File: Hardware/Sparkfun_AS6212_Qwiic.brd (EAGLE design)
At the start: 25.4 x 25.4 mm, 57 parts, among them J1 PTH, J2 QWIIC_RA, J3 QWIIC_RA, U2 AS6212

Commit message: Layout ready for review
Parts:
- removed JP6: JUMPER-SMT_3_1-NC_TRACE_NO-SILK, SparkFun-Jumpers:SMT-JUMPER_3_1-NC_TRACE_NO-SILK
- removed JP7: JUMPER-SMT_3_NO_NO_SILK, SparkFun-Jumpers:SMT-JUMPER_3_0-NO_TRACE_NO-SILK
- removed U$20: (no value), Labels:PWR-()-04
- removed U$21: (no value), Labels:I_SUPER2_C-()-04
- removed U$32, U$37: (no value), output:#ALRT#0
- removed U$42: (no value), buzzard_labels (26):0X480
- added JP10: JUMPER-SMT_3_1-NC_TRACE_NO-SILK, SparkFun-Jumpers:SMT-JUMPER_3_1-NC_TRACE_NO-SILK
- added JP11: JUMPER-SMT_3_NO_NO_SILK, SparkFun-Jumpers:SMT-JUMPER_3_0-NO_TRACE_NO-SILK
- added U$10: (no value), output:SDA6
- added U$11, U$12: (no value), output:#ALRT#AD1#12
- added U$13: (no value), output:VCC4
- added U$14, U$9: (no value), output:GND5
- added U$19: (no value), output:PWR12
- added U$4: (no value), output:#AD0#1
- added U$5: (no value), output:#AD1#1
- added U$6: (no value), output:SCL3
- U$1: device output:TEMPERATURE_SENSOR7 -> output:#LED#10
- U$16: device buzzard_labels (25):0X4A2 -> output:SENSOR8
- U$17: device buzzard_labels (25):0X4B3 -> output:TEMP9
- U$18: device buzzard_labels (1):ADDR0 -> output:0X4812
- U$2: device buzzard_labels (25):0X491 -> output:#I2C#11
- U$7: device Labels:INT-()-04 -> output:VCC4
- U$8: device buzzard_labels (5):LED0 -> output:DEFAULT#11
- moved R6 64.5 mm to (22.9, 19.6), turned to 180 degrees
- moved U$1 53.1 mm to (2.77, 7.44)
- moved U$3 50.1 mm to (4.65, 12.5)
- moved U$18 20.2 mm to (4.70, 9.60), turned to 0 degrees
- moved U$15 19.0 mm to (3.17, 17.3)
- moved U$17 18.9 mm to (4.62, 15.6), turned to 0 degrees
- moved R2 16.6 mm to (23.0, 17.8), turned to 180 degrees
- moved U$16 16.3 mm to (4.55, 14.2), turned to 0 degrees
- moved U$2 10.0 mm to (22.9, 7.57), turned to 0 degrees
- moved U$7 9.93 mm to (21.2, 20.3)
- moved LOGO1 8.20 mm to (10.6, 20.6)
- moved JP1 5.98 mm to (2.77, 5.71), turned to 180 degrees
- moved LOGO2 5.22 mm to (8.48, 18.1)
- moved JP4 3.55 mm to (17.4, 14.5), turned to 270 degrees
- moved U$8 2.82 mm to (4.57, 11.0)
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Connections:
- net ALERT/ADD1: now also JP10.2, JP11.2; no longer JP6.2, JP7.2
- net GND: now also JP11.3; no longer JP6.3
- net N$5: now also JP10.3; no longer JP7.1
- net SCL: now also JP10.1; no longer JP7.3
- net SDA: now also JP11.1; no longer JP6.1
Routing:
- net SCL: track 0.00 -> 63.3 mm, vias 0 -> 4
- net 3.3V: track 0.00 -> 61.5 mm, vias 0 -> 2
- net ALERT/ADD1: track 0.00 -> 60.3 mm, vias 0 -> 2
- net SDA: track 0.00 -> 48.9 mm, vias 0 -> 4
- net ADD0: track 0.00 -> 27.7 mm, vias 0 -> 1
- net N$7: track 0.00 -> 5.97 mm, vias 0 -> 1
- net N$3: track 0.00 -> 5.67 mm, vias 0 -> 1
- net N$5: track 0.00 -> 4.73 mm, vias 0 -> 1
- net N$2: track 0.00 -> 3.52 mm, vias 0 -> 1
- net N$8: track 0.00 -> 2.49 mm, vias 0 -> 1
- net N$1: track 0.00 -> 1.50 mm
- net GND: track 0.00 -> 1.14 mm, vias 0 -> 9
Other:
- outline, holes or cut-outs redrawn

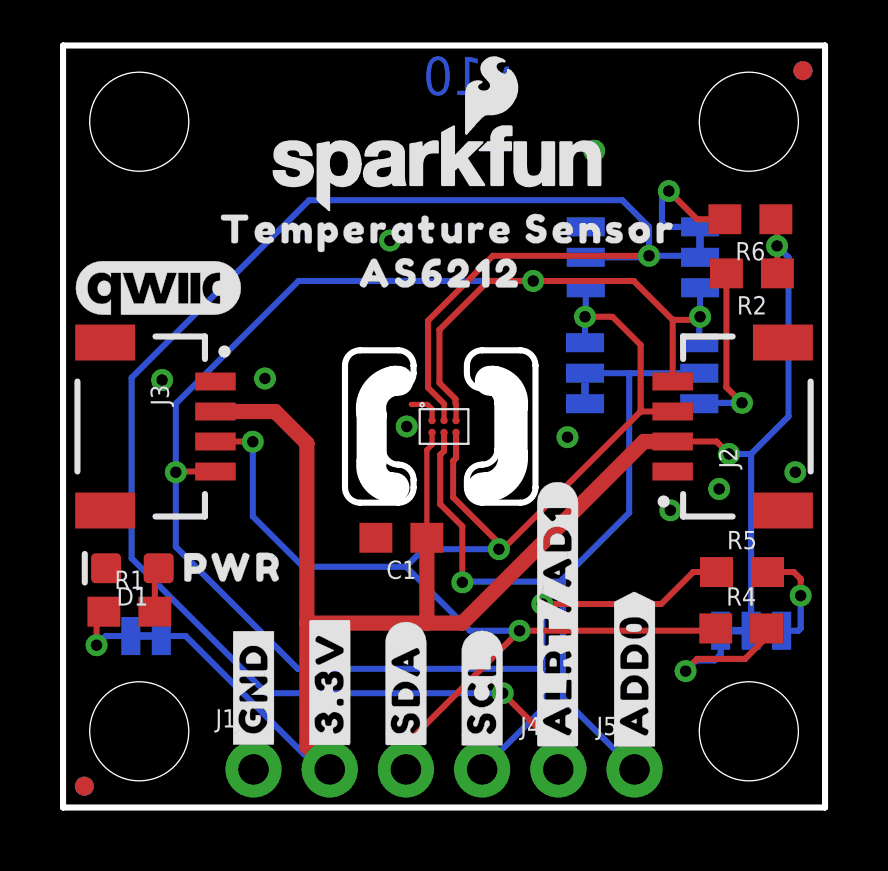
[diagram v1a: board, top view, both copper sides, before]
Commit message: my run of checklist catches
-silk outline of IC package increased to 8 mil
-approved DRC errors
-re-routed off IS to allow GND flow
-more GND stiching vias
-nudged some resistors away from standoff screw head
-updated 3-pad jumpers to latest in library to avoid access DRC errors
-added measures
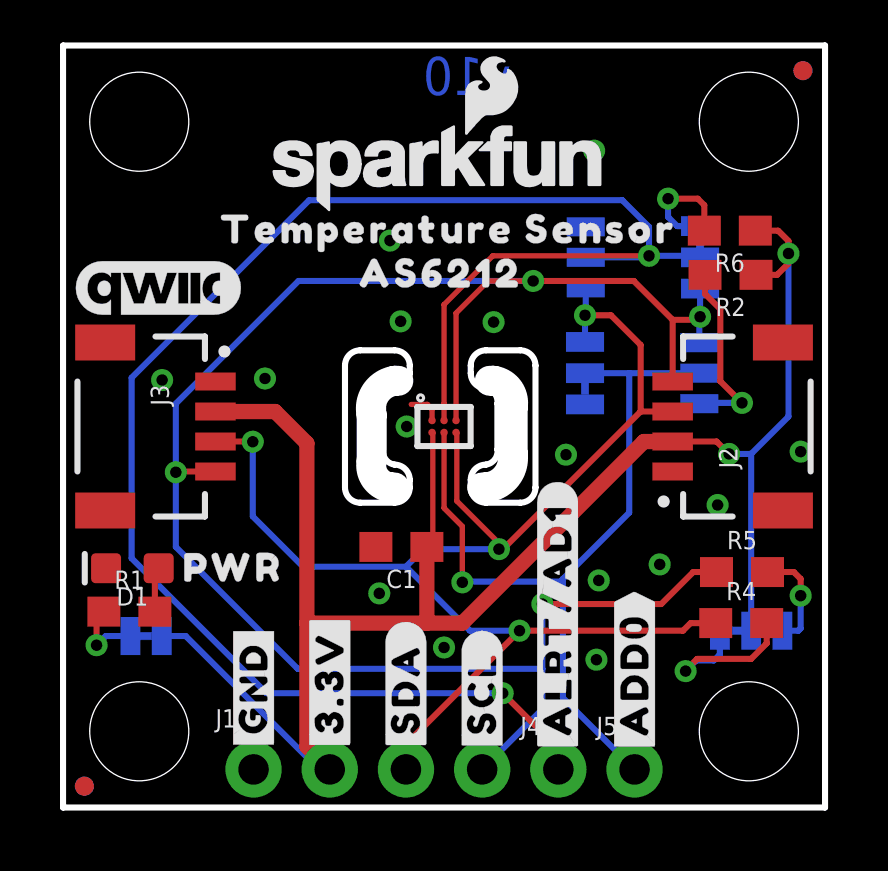
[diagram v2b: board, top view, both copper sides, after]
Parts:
- moved U$8 16.6 mm to (21.2, 10.9)
- moved U$18 16.5 mm to (21.2, 9.32)
- moved FRAME1 10.2 mm to (-7.62, -19.1)
- moved R6 0.78 mm to (22.2, 19.2)
- moved R2 0.71 mm to (22.3, 17.8)
- moved C1 0.30 mm to (11.3, 8.69)
- moved R4 0.18 mm to (22.6, 6.15)
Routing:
- net 3.3V: track 61.5 -> 62.4 mm
- net N$5: track 4.73 -> 3.95 mm
- net GND: vias 9 -> 15
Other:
- outline, holes or cut-outs redrawn
- board text added: "Measurement Units: INCHES"

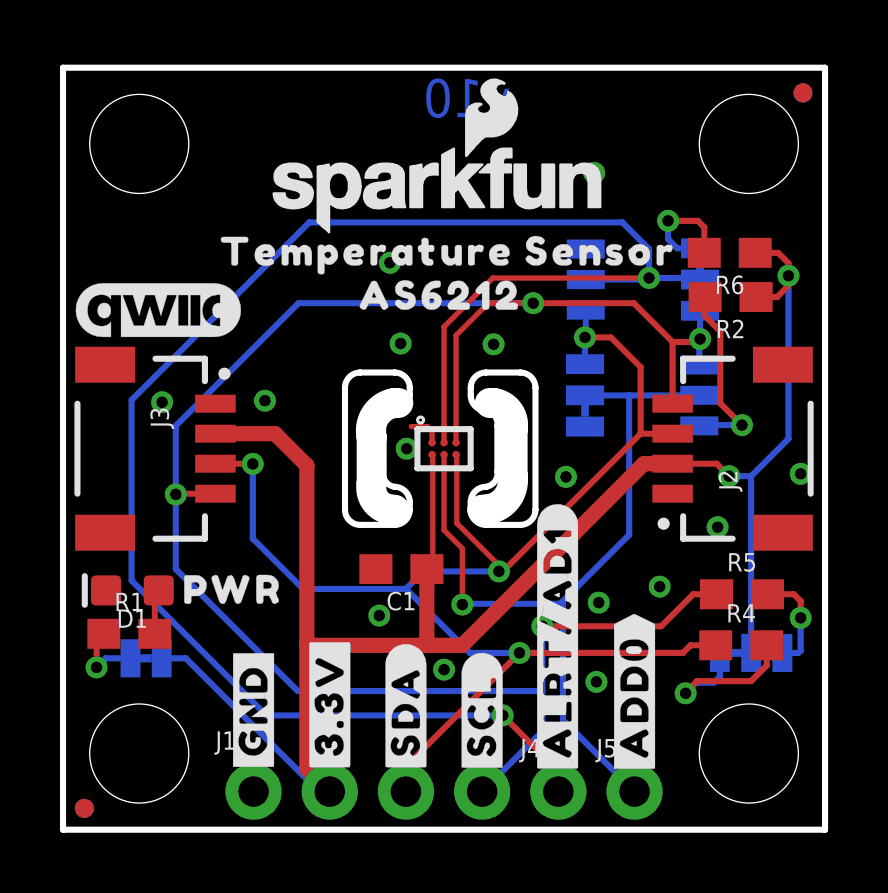
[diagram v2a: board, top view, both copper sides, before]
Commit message: design review group
-adjusted some traces and added more GND vias for return currents
-changed to 3V3 on label to avoid dot not printing nice
-GND symbols updated to new libraries
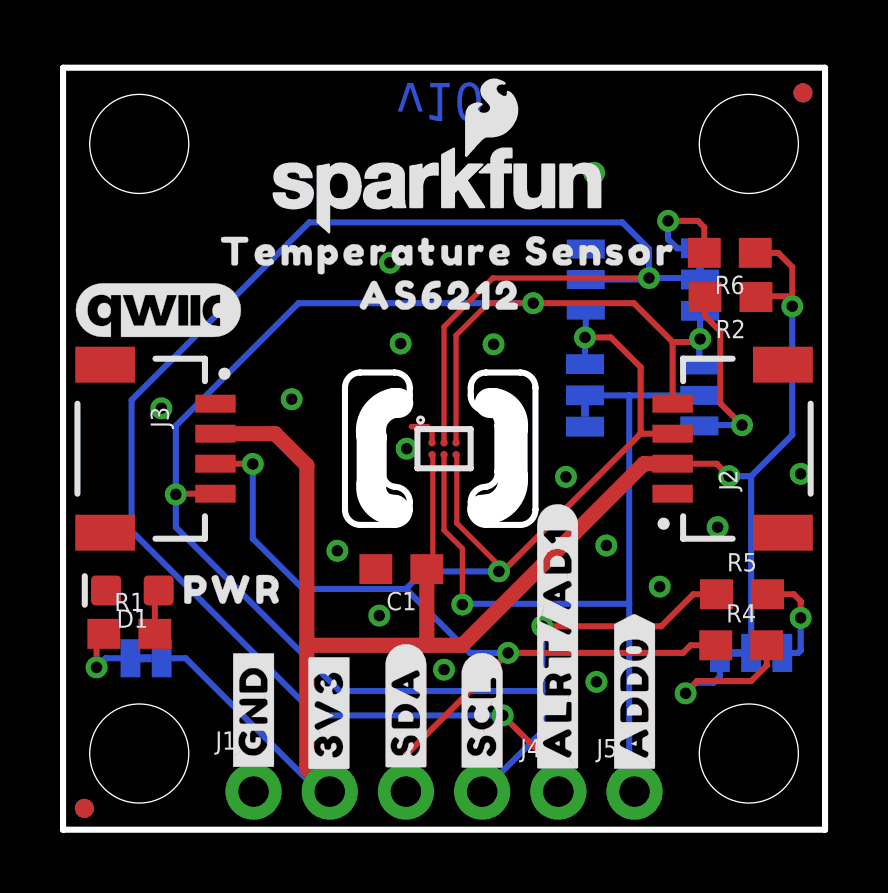
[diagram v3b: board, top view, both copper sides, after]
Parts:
- removed U$27, U$33: (no value), output:#3#3V#62131
- added U$20, U$21: (no value), output:#3V3#13
- JP2, JP3, JP8, JP9: device SparkFun:STAND-OFF -> SparkFun-Hardware:STAND-OFF
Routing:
- net ALERT/ADD1: track 59.8 -> 58.8 mm
- net SCL: track 62.8 -> 62.0 mm
- net GND: vias 15 -> 16
